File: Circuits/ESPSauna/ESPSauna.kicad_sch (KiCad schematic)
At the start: 44 parts, among them J1 AudioJack3, J2 Conn_01x04, Q1 AO3400A, Q2 AO3400A, U1 AP63203WU, U3 AM2302, U4 ESP32-DEVKIT-V1

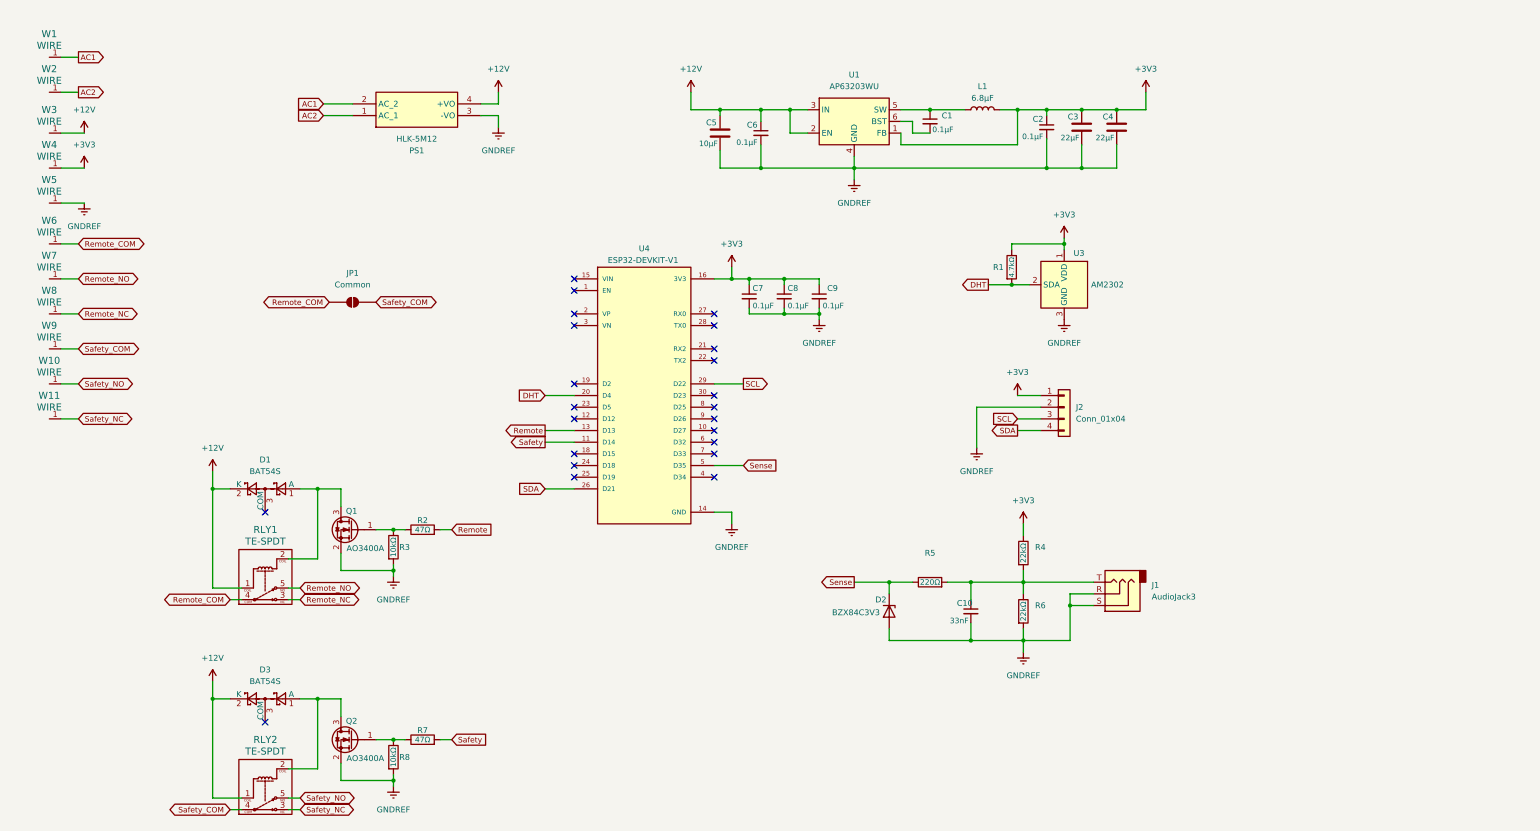
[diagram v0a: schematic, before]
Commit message: Updates to ESPSauna (fixing current clamp)
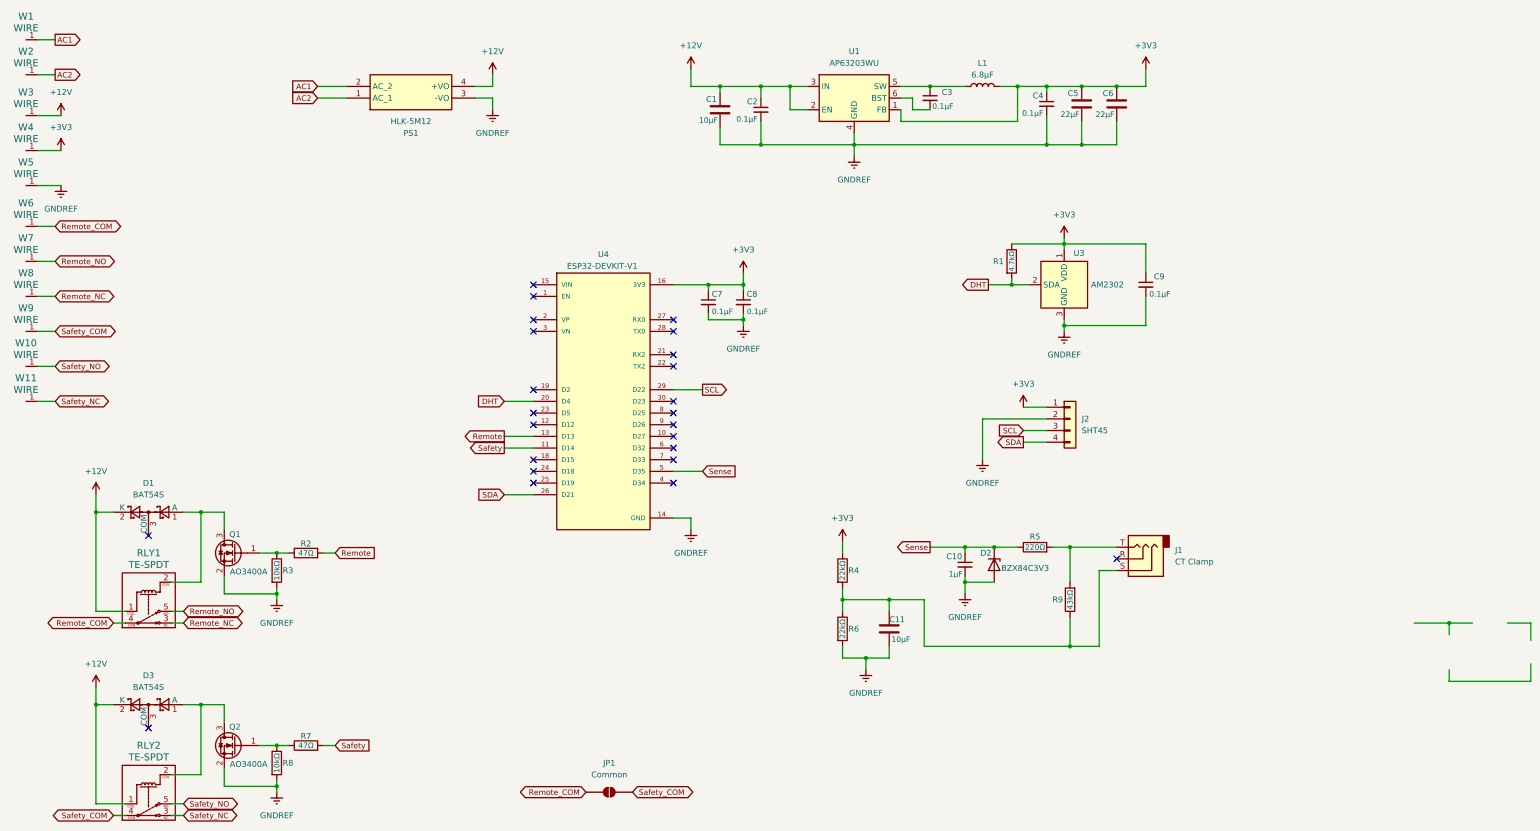
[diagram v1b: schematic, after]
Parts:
- added C11: 10μF, Capacitor_SMD:C_1206_3216Metric_Pad1.33x1.80mm_HandSolder, symbol Device:C
- added R9: 43kΩ, Resistor_THT:R_Axial_DIN0207_L6.3mm_D2.5mm_P10.16mm_Horizontal, symbol Device:R
- C10: value 33nF -> 1μF
- J1: value AudioJack3 -> CT Clamp
- J2: value Conn_01x04 -> SHT45
- renumbered C5 to C1, C6 to C2, C1 to C3, C2 to C4, C3 to C5, C4 to C6
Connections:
- net GND: now also C11.2; no longer J1.R, J1.S
- net Sense: now also C10.1
- new net: C11.1, J1.S, R4.2, R6.1, R9.1
- new net: J1.T, R5.2, R9.2
- no-connect marks 23 -> 24
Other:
- moved on the sheet: C1, C10, C2, C3, C4, C5, C6, C7, C8, C9, D1, D2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
